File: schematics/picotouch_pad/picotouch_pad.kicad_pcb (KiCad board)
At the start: 2 copper layers, 193 x 34 mm, 82 parts, among them SW1 1, SW10 1, SW11 1, SW12 1, SW13 1, SW14 1, SW15 1, SW16 1, SW17 1, SW18 1, SW19 1, SW2 1, SW20 1, SW21 1, SW22 1, SW23 1, SW3 1, SW4 1, SW5 1, SW6 1, SW7 1, SW8 1, SW9 1, U1 Pico

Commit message: files as sent to fab
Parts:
- added G***: LOGO, LOGO, F.Cu at (109.1, 45.4)
- moved TP1 0.10 mm to (20.9, 59.4)
- moved TP3 0.10 mm to (23.5, 59.4)
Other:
- board size 193 x 34 mm -> 190 x 34 mm
- board text added: "JLCJLCJLCJLC"
- board text added: "picotouch_pad - USB MIDI controller / macropad 5 Sep 2024 - @todbot / Tod Kurt github.com/todbot/picotouch_pad Uses Pico RP2040"

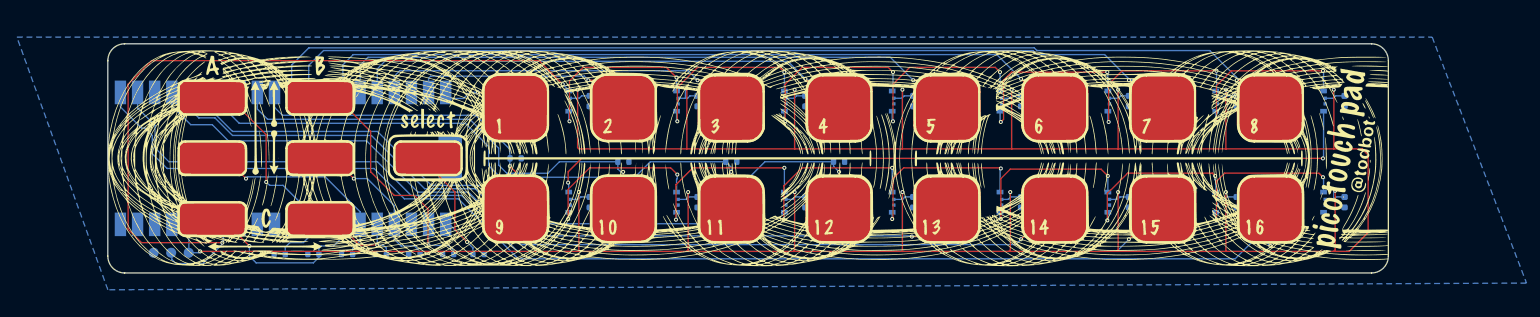
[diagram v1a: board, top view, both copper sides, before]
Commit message: new pcb with sk6812side
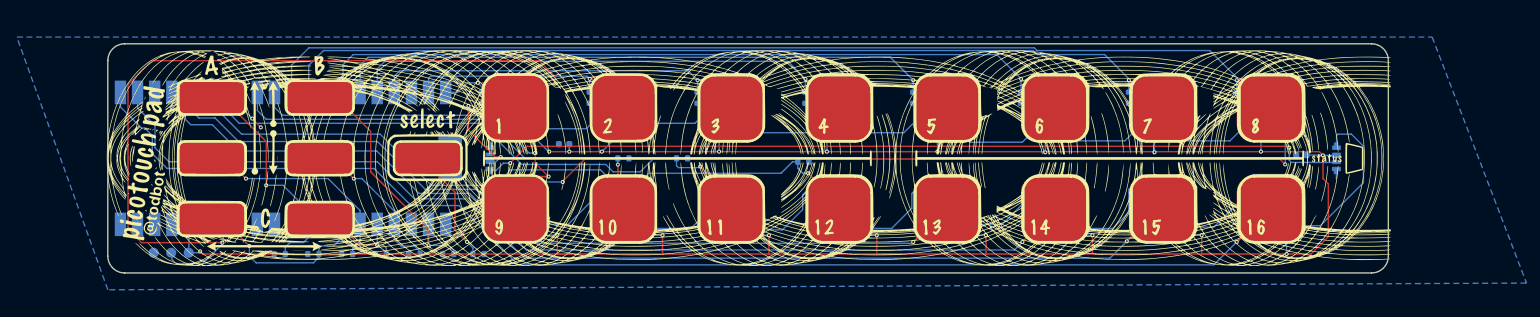
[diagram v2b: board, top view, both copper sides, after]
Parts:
- added C17: 100n, Capacitor_SMD:C_0603_1608Metric, B.Cu at (191.2, 44.9)
- added C18: 100n, Capacitor_SMD:C_0603_1608Metric, B.Cu at (81.8, 43.3)
- added LED17: SK6812SIDE, todbot_stuff:LED-SMD_4P-L4.0-W1.6-L-keepoutrev, B.Cu at (196.4, 45.4)
- added LED18: SK6812SIDE, todbot_stuff:LED-SMD_4P-L4.0-W1.6-L-keepoutrev, B.Cu at (70.8, 45.4)
- LED1, LED10, LED11, LED12, LED13, LED14, LED15, LED16, LED2, LED3, LED4, LED5, LED6, LED7, LED8, LED9: value SK6805-EC3210R -> SK6812SIDE; footprint todbot_stuff:LED-SMD_4P-L3.2-W1.5_SK6805-EC3210R-keepout -> todbot_stuff:LED-SMD_4P-L4.0-W1.6-L-keepoutrev
- moved C1 11.0 mm to (74.6, 36.4)
- moved C3 11.0 mm to (106.6, 36.4)
- moved C4 11.0 mm to (122.6, 36.4)
- moved C5 11.0 mm to (138.6, 36.4)
- moved C6 11.0 mm to (154.6, 36.4)
- moved C8 11.0 mm to (186.6, 36.4)
- moved C11 11.0 mm to (106.6, 52.2)
- moved C12 11.0 mm to (122.6, 52.2)
- moved C13 11.0 mm to (138.6, 52.2)
- moved C14 11.0 mm to (154.6, 52.2)
- moved C9 11.0 mm to (74.6, 52.2)
- moved C10 11.0 mm to (90.6, 52.0)
- moved C2 10.8 mm to (90.8, 36.4)
- moved C7 10.8 mm to (170.8, 36.4)
- moved C15 10.8 mm to (170.8, 52.2)
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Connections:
- LED1 pad 1: GND -> /LED_DAT
- LED1 pad 2: Net-(LED1-DOUT) -> +3.3V
- LED1 pad 3: /LED_DAT -> Net-(LED1-DOUT)
- LED1 pad 4: +3.3V -> GND
- LED10 pad 1: GND -> Net-(LED10-DIN)
- LED10 pad 2: Net-(LED10-DOUT) -> +3.3V
- LED10 pad 3: Net-(LED10-DIN) -> Net-(LED10-DOUT)
- LED10 pad 4: +3.3V -> GND
- LED11 pad 1: GND -> Net-(LED10-DOUT)
- LED11 pad 2: Net-(LED11-DOUT) -> +3.3V
- LED11 pad 3: Net-(LED10-DOUT) -> Net-(LED11-DOUT)
- LED11 pad 4: +3.3V -> GND
- LED12 pad 1: GND -> Net-(LED11-DOUT)
- LED12 pad 2: Net-(LED12-DOUT) -> +3.3V
- LED12 pad 3: Net-(LED11-DOUT) -> Net-(LED12-DOUT)
- LED12 pad 4: +3.3V -> GND
- LED13 pad 1: GND -> Net-(LED12-DOUT)
- LED13 pad 2: Net-(LED13-DOUT) -> +3.3V
- LED13 pad 3: Net-(LED12-DOUT) -> Net-(LED13-DOUT)
- LED13 pad 4: +3.3V -> GND
- LED14 pad 1: GND -> Net-(LED13-DOUT)
- LED14 pad 2: Net-(LED14-DOUT) -> +3.3V
- LED14 pad 3: Net-(LED13-DOUT) -> Net-(LED14-DOUT)
- LED14 pad 4: +3.3V -> GND
- LED15 pad 1: GND -> Net-(LED14-DOUT)
- LED15 pad 2: Net-(LED15-DOUT) -> +3.3V
- LED15 pad 3: Net-(LED14-DOUT) -> Net-(LED15-DOUT)
- LED15 pad 4: +3.3V -> GND
- LED16 pad 1: GND -> Net-(LED15-DOUT)
- LED16 pad 2: unconnected-(LED16-DOUT-Pad2) -> +3.3V
- LED16 pad 3: Net-(LED15-DOUT) -> Net-(LED16-DOUT)
- LED16 pad 4: +3.3V -> GND
- LED2 pad 1: GND -> Net-(LED1-DOUT)
- LED2 pad 2: Net-(LED2-DOUT) -> +3.3V
- LED2 pad 3: Net-(LED1-DOUT) -> Net-(LED2-DOUT)
- LED2 pad 4: +3.3V -> GND
- LED3 pad 1: GND -> Net-(LED2-DOUT)
- LED3 pad 2: Net-(LED3-DOUT) -> +3.3V
- LED3 pad 3: Net-(LED2-DOUT) -> Net-(LED3-DOUT)
- LED3 pad 4: +3.3V -> GND
- LED4 pad 1: GND -> Net-(LED3-DOUT)
- LED4 pad 2: Net-(LED4-DOUT) -> +3.3V
- LED4 pad 3: Net-(LED3-DOUT) -> Net-(LED4-DOUT)
- LED4 pad 4: +3.3V -> GND
- LED5 pad 1: GND -> Net-(LED4-DOUT)
- LED5 pad 2: Net-(LED5-DOUT) -> +3.3V
- LED5 pad 3: Net-(LED4-DOUT) -> Net-(LED5-DOUT)
- LED5 pad 4: +3.3V -> GND
- LED6 pad 1: GND -> Net-(LED5-DOUT)
- LED6 pad 2: Net-(LED6-DOUT) -> +3.3V
- LED6 pad 3: Net-(LED5-DOUT) -> Net-(LED6-DOUT)
- LED6 pad 4: +3.3V -> GND
- LED7 pad 1: GND -> Net-(LED6-DOUT)
- LED7 pad 2: Net-(LED7-DOUT) -> +3.3V
- LED7 pad 3: Net-(LED6-DOUT) -> Net-(LED7-DOUT)
- LED7 pad 4: +3.3V -> GND
- LED8 pad 1: GND -> Net-(LED7-DOUT)
- LED8 pad 2: Net-(LED8-DOUT) -> +3.3V
- LED8 pad 3: Net-(LED7-DOUT) -> Net-(LED8-DOUT)
- LED8 pad 4: +3.3V -> GND
- LED9 pad 1: GND -> Net-(LED8-DOUT)
- LED9 pad 2: Net-(LED10-DIN) -> +3.3V
- LED9 pad 3: Net-(LED8-DOUT) -> Net-(LED10-DIN)
- LED9 pad 4: +3.3V -> GND
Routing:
- net Net-(LED17-DOUT): track 0.00 -> 129.2 mm, vias 0 -> 2
- net +3.3V: track 519.8 -> 574.1 mm, vias 17 -> 21
- net Net-(LED16-DOUT): track 0.00 -> 29.5 mm
- net GND: track 0.67 -> 25.7 mm, vias 0 -> 2
- net /TOUCH9: track 48.1 -> 57.7 mm, vias 1 -> 2
- net /TOUCH10: track 68.7 -> 61.0 mm
- net Net-(LED5-DOUT): track 26.7 -> 33.9 mm, vias 2 -> 0
- net Net-(LED6-DOUT): track 27.1 -> 34.2 mm, vias 2 -> 0
- net /TOUCH12: track 112.5 -> 105.6 mm
- net /TOUCH7: track 144.4 -> 138.3 mm
- net Net-(LED7-DOUT): track 26.8 -> 32.4 mm, vias 2 -> 0
- net /TOUCH11: track 90.1 -> 86.4 mm
- net Net-(LED3-DOUT): track 27.2 -> 30.8 mm, vias 2 -> 0
- net Net-(LED14-DOUT): track 25.1 -> 28.1 mm, vias 2 -> 0
- net Net-(LED4-DOUT): track 27.1 -> 30.0 mm, vias 2 -> 0
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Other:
- board text added: "picotouch_pad2a - USB MIDI controller / macropad 9 Sep 2024 - @todbot / Tod Kurt github.com/todbot/picotouch_pad Uses Pico RP2040"
- board text removed: "picotouch_pad - USB MIDI controller / macropad 5 Sep 2024 - @todbot / Tod Kurt github.com/todbot/picotouch_pad Uses Pico RP2040"

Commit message: add battery circuit
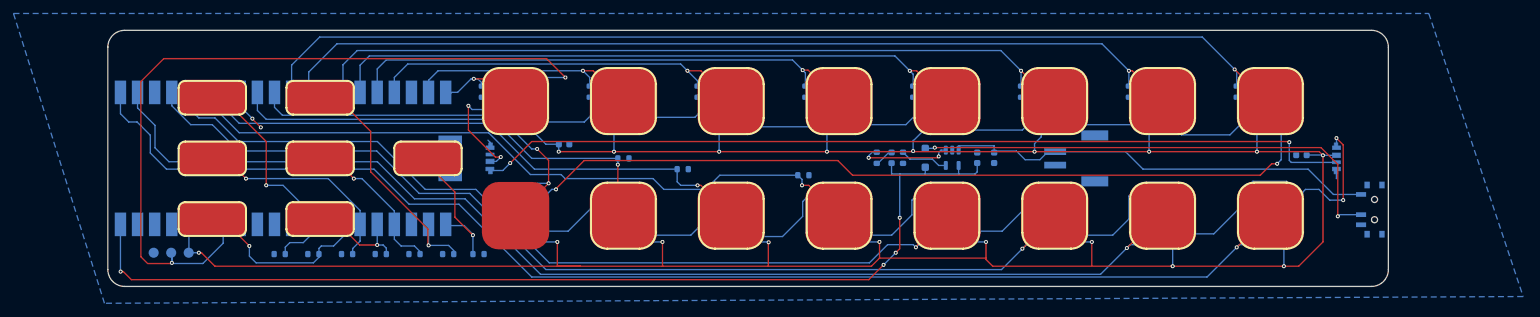
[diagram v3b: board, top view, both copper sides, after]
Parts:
- removed G***: LOGO, LOGO
- added C19: 10uF, Capacitor_SMD:C_0603_1608Metric, B.Cu at (145.6, 45.3)
- added C20: 10uF, Capacitor_SMD:C_0603_1608Metric, B.Cu at (143.1, 45.3)
- added D1: orange, LED_SMD:LED_0603_1608Metric, B.Cu at (130.4, 45.3)
- added D2: MBR120, Diode_SMD:D_SOD-123F, B.Cu at (135.4, 45.3)
- added R24: 5.1k, Resistor_SMD:R_0603_1608Metric, B.Cu at (132.1, 45.3)
- added R25: 5.1k, Resistor_SMD:R_0603_1608Metric, B.Cu at (128.2, 45.3)
- added SW24: SSSS811101, easyeda2kicad:SW-SMD_SSSS811101, B.Cu at (201.6, 53.0)
- added U2: MCP73831-2-OT, Package_TO_SOT_SMD:SOT-23-5, B.Cu at (139.4, 45.3)
- added X1: AFC20-S02ACA-00, easyeda2kicad:CONN-SMD_AFC20-S02ACA-00, B.Cu at (157.6, 45.4)
- moved R12 2.00 mm to (117.3, 47.9)
- moved R11 1.60 mm to (99.4, 47.0)
- moved C10 1.00 mm to (90.6, 53.0)
- moved C11 1.00 mm to (106.6, 53.2)
- moved C12 1.00 mm to (122.6, 53.2)
- moved C13 1.00 mm to (138.6, 53.2)
- moved C14 1.00 mm to (154.6, 53.2)
- moved C15 1.00 mm to (170.8, 53.2)
- moved C16 1.00 mm to (187.6, 53.2)
- moved LED10 1.00 mm to (94.2, 52.9)
- moved LED11 1.00 mm to (110.2, 52.9)
- moved LED12 1.00 mm to (126.2, 52.9)
- moved LED13 1.00 mm to (142.2, 52.9)
- moved LED14 1.00 mm to (158.2, 52.9)
- moved LED15 1.00 mm to (174.2, 52.9)
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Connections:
- U1 pad 40: unconnected-(U1-VBUS-Pad40) -> +5V
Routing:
- net +5V: track 0.00 -> 155.5 mm, vias 0 -> 4
- net Net-(D2-A): track 0.00 -> 73.9 mm, vias 0 -> 2
- net +BATT: track 0.00 -> 65.0 mm
- net Net-(U2-STAT): track 0.00 -> 14.0 mm, vias 0 -> 2
- net Net-(LED16-DOUT): track 29.5 -> 21.7 mm, vias 0 -> 2
- net Net-(U2-PROG): track 0.00 -> 7.16 mm
- net /TOUCH10: track 61.0 -> 67.1 mm
- net /TOUCH19: track 26.9 -> 21.4 mm
- net /TOUCH20: track 20.2 -> 15.2 mm
- net /LED_DAT: track 119.8 -> 116.4 mm
- net Net-(D1-K): track 0.00 -> 2.87 mm
- net /TOUCH11: track 86.4 -> 84.5 mm
- net /TOUCH13: track 127.9 -> 129.8 mm
- net Net-(LED6-DOUT): track 34.2 -> 32.4 mm
- net /TOUCH12: track 105.6 -> 103.9 mm
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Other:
- board size 190 x 34 mm -> 190 x 38 mm
- board text added: "picotouch_pad - USB MIDI controller / macropad 15 Sep 2024 - @todbot / Tod Kurt github.com/todbot/picotouch_pad Uses Pico RP2040"
- board text removed: "picotouch_pad2a - USB MIDI controller / macropad 9 Sep 2024 - @todbot / Tod Kurt github.com/todbot/picotouch_pad Uses Pico RP2040"

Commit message: add battery circuit
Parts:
- moved R11 0.80 mm to (99.4, 47.8)
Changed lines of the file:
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@@
 	(footprint "Resistor_SMD:R_0603_1608Metric"
 		(layer "B.Cu")
-		(at 99.43 46.99)
+		(at 99.43 47.79)
 		(descr "Resistor SMD 0603 (1608 Metric), square (rectangular) end terminal, IPC_7351 nominal, (Body size source: IPC-SM-782 page 72, https://www.pcb-3d.com/wordpress/wp-content/uploads/ipc-sm-782a_amendment_1_and_2.pdf), generated with kicad-footprint-generator")
 		(tags "resistor")
@@
 		(tags "capacitor")
 		(property "Reference" "C19"
-			(at -2.1125 -0.7925 180)
-			(layer "B.SilkS")
+			(at -2.1125 -0.7925 -180)
+			(layer "F.SilkS")
 			(effects
 				(font
@@
 					(thickness 0.15)
 				)
-				(justify mirror)
 			)
 		)
 		(property "Value" "10uF"
-			(at 0 -1.43 90)
-			(layer "B.Fab")
+			(at 0 -1.43 -90)
+			(layer "F.Fab")
 			(effects
 				(font
@@
 					(thickness 0.15)
 				)
-				(justify mirror)
 			)
 		)
@@
 	)
 	(segment
-		(start 135.63 40.79)
-		(end 135.63 37.725)
-		(width 0.2)
-		(layer "B.Cu")
-		(net 2)
-	)
-	(segment
 		(start 120.83 35.7)
 		(end 121.805 34.725)
@@
 	)
 	(segment
+		(start 136.23 40.19)
+		(end 136.23 36.39)
+		(width 0.2)
+		(layer "B.Cu")
+		(net 2)
+	)
+	(segment
 		(start 72.63 35.39)
 		(end 72.63 38.14)
@@
 	)
 	(segment
-		(start 142.22 35.45)
-		(end 140.58 35.45)
-		(width 0.2)
-		(layer "B.Cu")
-		(net 2)
-	)
-	(segment
 		(start 169.295 34.725)
 		(end 170.83 34.725)
@@
 	(segment
 		(start 139.855 34.725)
-		(end 138.63 34.725)
+		(end 140.58 35.45)
 		(width 0.2)
 		(layer "B.Cu")
@@
 	)
 	(segment
+		(start 133.63 42.79)
+		(end 136.23 40.19)
+		(width 0.2)
+		(layer "B.Cu")
+		(net 2)
+	)
+	(segment
 		(start 91.83 52.215)
 		(end 92.055 52.44)
@@
 	)
 	(segment
-		(start 135.63 37.725)
-		(end 138.63 34.725)
+		(start 172.58 35.45)
+		(end 171.855 34.725)
 		(width 0.2)
 		(layer "B.Cu")
@@
 	)
 	(segment
-		(start 172.58 35.45)
-		(end 171.855 34.725)
+		(start 110.22 52.44)
+		(end 108.03 52.44)
 		(width 0.2)
 		(layer "B.Cu")
@@
 	)
 	(segment
-		(start 110.22 52.44)
-		(end 108.03 52.44)
+		(start 136.23 36.39)
+		(end 137.895 34.725)
 		(width 0.2)
 		(layer "B.Cu")
@@
 	)
 	(segment
-		(start 133.63 42.79)
-		(end 135.63 40.79)
-		(width 0.2)
-		(layer "B.Cu")
-		(net 2)
-	)
-	(segment
 		(start 158.22 35.45)
 		(end 156.78 35.45)
@@
 	)
 	(segment
+		(start 140.58 35.45)
+		(end 142.22 35.45)
+		(width 0.2)
+		(layer "B.Cu")
+		(net 2)
+	)
+	(segment
 		(start 133.6175 44.3025)
 		(end 133.6175 42.7025)
@@
 	)
 	(segment
+		(start 137.895 34.725)
+		(end 139.855 34.725)
+		(width 0.2)
+		(layer "B.Cu")
+		(net 2)
+	)
+	(segment
 		(start 89.23 44.39)
 		(end 89.23 35.59)
@@
 	)
 	(segment
-		(start 140.58 35.45)
-		(end 139.855 34.725)
-		(width 0.2)
-		(layer "B.Cu")
-		(net 2)
-	)
-	(segment
 		(start 77.03 36.79)
 		(end 77.03 39.39)
@@
 	)
 	(segment
-		(start 77.43 46.99)
-		(end 70.63 40.19)
+		(start 98.605 48.865)
+		(end 98.605 47.79)
 		(width 0.2)
 		(layer "B.Cu")
@@
 	)
 	(segment
-		(start 33.63 40.19)
-		(end 31.24 37.8)
+		(start 31.24 37.8)
+		(end 31.24 36.5)
 		(width 0.2)
 		(layer "B.Cu")
@@
 	)
 	(segment
-		(start 101.63 49.39)
-		(end 99.13 49.39)
+		(start 99.13 49.39)
+		(end 98.605 48.865)
 		(width 0.2)
 		(layer "B.Cu")
@@
 	)
 	(segment
-		(start 99.13 49.39)
-		(end 98.605 48.865)
+		(start 77.43 46.99)
+		(end 70.63 40.19)
 		(width 0.2)
 		(layer "B.Cu")
@@
 	)
 	(segment
-		(start 70.63 40.19)
-		(end 33.63 40.19)
+		(start 88.63 46.99)
+		(end 77.43 46.99)
 		(width 0.2)
 		(layer "B.Cu")
@@
 	)
 	(segment
-		(start 31.24 37.8)
-		(end 31.24 36.5)
+		(start 33.63 40.19)
+		(end 31.24 37.8)
 		(width 0.2)
 		(layer "B.Cu")
@@
 	)
 	(segment
-		(start 98.605 46.99)
-		(end 77.43 46.99)
+		(start 101.63 49.39)
+		(end 99.13 49.39)
 		(width 0.2)
 		(layer "B.Cu")
@@
 	)
 	(segment
-		(start 98.605 48.865)
-		(end 98.605 46.99)
+		(start 70.63 40.19)
+		(end 33.63 40.19)
+		(width 0.2)
+		(layer "B.Cu")
+		(net 38)
+	)
+	(segment
+		(start 89.43 47.79)
+		(end 88.63 46.99)
+		(width 0.2)
+		(layer "B.Cu")
+		(net 38)
+	)
+	(segment
+		(start 98.605 47.79)
+		(end 89.43 47.79)
 		(width 0.2)
 		(layer "B.Cu")
@@
 	)
 	(segment
-		(start 95.03 48.39)
-		(end 96.63 49.99)
+		(start 28.7 37.46)
+		(end 29.63 38.39)
 		(width 0.2)
 		(layer "B.Cu")
@@
 	)
 	(segment
-		(start 33.63 41.59)
-		(end 70.63 41.59)
+		(start 76.83 47.79)
+		(end 81.378529 47.79)
 		(width 0.2)
 		(layer "B.Cu")
@@
 	)
 	(segment
-		(start 30.43 38.39)
-		(end 33.63 41.59)
+		(start 117.13 49.39)
+		(end 117.13 48.515)
 		(width 0.2)
 		(layer "B.Cu")
@@
 	)
 	(segment
-		(start 117.13 49.39)
-		(end 117.13 48.515)
+		(start 82.578529 48.99)
+		(end 95.63 48.99)
 		(width 0.2)
 		(layer "B.Cu")
@@
 	)
 	(segment
-		(start 81.378529 47.79)
-		(end 81.978529 48.39)
+		(start 95.63 48.99)
+		(end 97.23 50.59)
 		(width 0.2)
 		(layer "B.Cu")
@@
 	)
 	(segment
-		(start 102.83 49.99)
-		(end 104.93 47.89)
+		(start 29.63 38.39)
+		(end 30.43 38.39)
 		(width 0.2)
 		(layer "B.Cu")
@@
 	)
 	(segment
-		(start 76.83 47.79)
-		(end 81.378529 47.79)
+		(start 70.63 41.59)
+		(end 76.83 47.79)
 		(width 0.2)
 		(layer "B.Cu")
@@
 	)
 	(segment
-		(start 96.63 49.99)
-		(end 102.83 49.99)
+		(start 33.63 41.59)
+		(end 70.63 41.59)
 		(width 0.2)
 		(layer "B.Cu")
@@
 	)
 	(segment
-		(start 29.63 38.39)
-		(end 30.43 38.39)
+		(start 97.23 50.59)
+		(end 102.23 50.59)
 		(width 0.2)
 		(layer "B.Cu")
@@
 	)
 	(segment
-		(start 81.978529 48.39)
-		(end 95.03 48.39)
+		(start 102.23 50.59)
+		(end 104.93 47.89)
 		(width 0.2)
 		(layer "B.Cu")
@@
 	)
 	(segment
-		(start 28.7 37.46)
-		(end 29.63 38.39)
+		(start 81.378529 47.79)
+		(end 82.578529 48.99)
 		(width 0.2)
 		(layer "B.Cu")
@@
 	)
 	(segment
-		(start 70.63 41.59)
-		(end 76.83 47.79)
+		(start 30.43 38.39)
+		(end 33.63 41.59)
 		(width 0.2)
 		(layer "B.Cu")
@@
 	)
 	(segment
-		(start 77.03 62.99)
-		(end 66.23 52.19)
+		(start 20.43 41.948578)
+		(end 18.471422 39.99)
 		(width 0.2)
 		(layer "B.Cu")
@@
 	)
 	(segment
-		(start 20.43 44.59)
-		(end 20.43 41.948578)
+		(start 176.83 63.39)
+		(end 77.43 63.39)
 		(width 0.2)
 		(layer "B.Cu")
@@
 	)
 	(segment
-		(start 20.43 41.948578)
-		(end 18.471422 39.99)
+		(start 22.83 46.99)
+		(end 20.43 44.59)
 		(width 0.2)
 		(layer "B.Cu")
@@
 	)
 	(segment
-		(start 16 38.76)
-		(end 16 36.5)
+		(start 181.63 58.59)
+		(end 176.83 63.39)
 		(width 0.2)
 		(layer "B.Cu")
@@
 	)
 	(segment
-		(start 17.23 39.99)
-		(end 16 38.76)
+		(start 66.23 52.19)
+		(end 58.83 52.19)
 		(width 0.2)
 		(layer "B.Cu")
@@
 	)
 	(segment
-		(start 66.23 52.19)
-		(end 58.83 52.19)
+		(start 16 38.76)
+		(end 16 36.5)
 		(width 0.2)
 		(layer "B.Cu")
@@
 	)
 	(segment
-		(start 22.83 46.99)
-		(end 20.43 44.59)
+		(start 77.43 63.39)
+		(end 66.23 52.19)
 		(width 0.2)
 		(layer "B.Cu")
@@
 	)
 	(segment
-		(start 177.23 62.99)
-		(end 77.03 62.99)
+		(start 17.23 39.99)
+		(end 16 38.76)
 		(width 0.2)
 		(layer "B.Cu")
@@
 	)
 	(segment
-		(start 181.63 58.59)
-		(end 177.23 62.99)
+		(start 20.43 44.59)
+		(end 20.43 41.948578)
 		(width 0.2)
 		(layer "B.Cu")

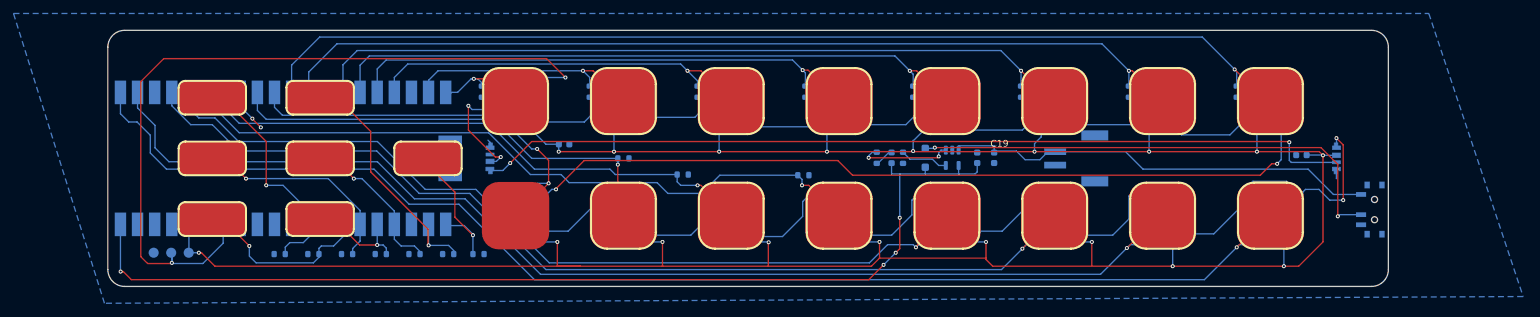
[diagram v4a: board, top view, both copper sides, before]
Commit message: add midi out
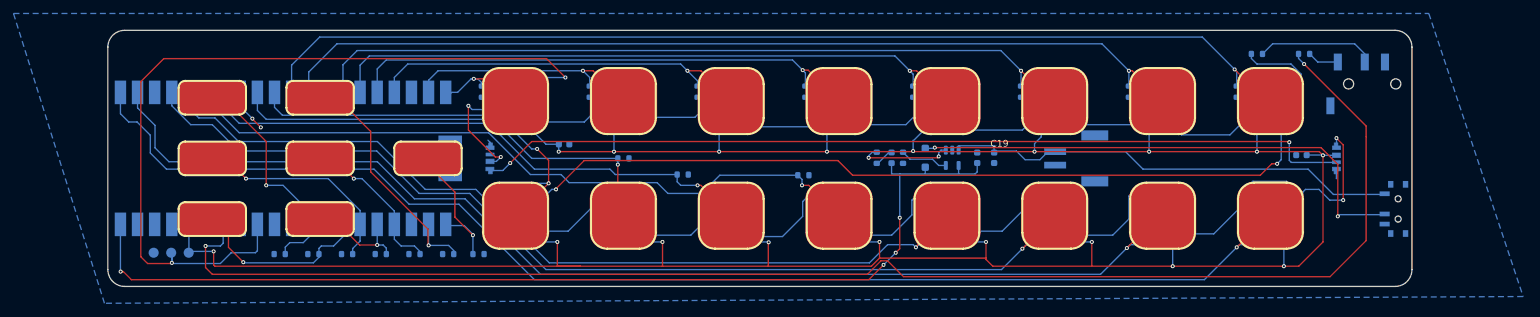
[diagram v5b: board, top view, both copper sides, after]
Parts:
- added J1: AudioJack4, todbot_stuff:Jack_3.5mm_PJ320D_Horizontal, B.Cu at (200.5, 34.3)
- added R26: 10, Resistor_SMD:R_0603_1608Metric, B.Cu at (191.6, 29.9)
- added R27: 33, Resistor_SMD:R_0603_1608Metric, B.Cu at (184.6, 29.9)
- moved SW24 3.50 mm to (205.1, 52.9)
- moved C16 1.00 mm to (186.6, 53.2)
- moved C15 0.20 mm to (170.6, 53.2)
- moved C7 0.20 mm to (170.6, 35.5)
- moved C2 0.20 mm to (90.6, 35.5)
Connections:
- U1 pad 32: unconnected-(U1-GPIO27_ADC1-Pad32) -> /LED_DAT
- U1 pad 34: /LED_DAT -> /MIDI_OUT
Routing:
- net /MIDI_OUT: track 0.00 -> 218.2 mm, vias 0 -> 2
- net Net-(J1-PadR1): track 0.00 -> 17.6 mm
- net +3.3V: track 574.8 -> 589.4 mm
- net /LED_DAT: track 116.4 -> 122.1 mm
- net Net-(J1-PadT): track 0.00 -> 4.67 mm
- net Net-(D2-A): track 73.9 -> 77.5 mm
- net +BATT: track 65.0 -> 68.5 mm
- net /TOUCH22: track 28.1 -> 29.1 mm
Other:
- board size 190 x 38 mm -> 193.5 x 38 mm

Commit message: cleanup
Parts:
- moved R25 4.59 mm to (123.6, 45.4)
- moved D1 3.79 mm to (126.6, 45.4)
- moved R24 2.49 mm to (129.6, 45.4)
- moved C19 1.00 mm to (146.6, 45.4)
- moved D2 0.79 mm to (134.6, 45.4)
- moved R10 0.60 mm to (91.2, 45.4)
- moved C20 0.51 mm to (143.6, 45.4)
- moved U2 0.23 mm to (139.6, 45.4)
- renumbered SW1 to PAD1, SW10 to PAD10, SW11 to PAD11, SW12 to PAD12, SW13 to PAD13, SW14 to PAD14, SW15 to PAD15, SW16 to PAD16, SW17 to PAD17, SW18 to PAD18, SW19 to PAD19, SW2 to PAD2, SW20 to PAD20, SW21 to PAD21, SW22 to PAD22, SW23 to PAD23, SW3 to PAD3, SW4 to PAD4, SW5 to PAD5, SW6 to PAD6, SW7 to PAD7, SW8 to PAD8, SW9 to PAD9, SW24 to SW1
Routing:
- net Net-(U2-STAT): track 14.0 -> 20.0 mm
- net +5V: track 155.5 -> 160.9 mm
- net +3.3V: track 589.4 -> 592.7 mm
- net Net-(U2-PROG): track 7.16 -> 9.61 mm
- net /LED_DAT: track 122.1 -> 119.9 mm
- net /TOUCH10: track 67.1 -> 68.5 mm
- net Net-(D1-K): track 2.87 -> 3.84 mm
- net Net-(LED8-DOUT): track 124.4 -> 123.8 mm
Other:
- board text added: "MIDI OUT TRS-A"
